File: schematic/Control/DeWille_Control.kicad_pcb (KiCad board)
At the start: 4 copper layers, 95 x 76.2 mm, 145 parts, among them J101 HN2x10, J102 HN2x10, J103 HN2x10, J201 SMA F ST PCB, J202 SMA F ST PCB, J501 Micro USB - KMMVX-SMT-BS-BTR, U201 KC2520K22.5792C1GE00, U202 KC2520K24.576C1GE00, U203 Si5344, U204 TPS79333-EP, U205 TPS73633DCQ, U206 TPS73618DCQ, U207 TPS79333-EP, U301 ESP32DevKit, U401 LFXP2-5E-5TN144, U402 IS61WV25616E, U403 TPS73633DCQ, U404 TPS79333-EP, U405 TLV74112PDBVR, U501 93C46C, U502 FT2232H, Y201 CX3225SB48, Y501 12MHz

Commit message: Interim commit
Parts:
- removed D501: Green, LED_SMD:LED_0805_2012Metric
- removed D502: Red, LED_SMD:LED_0805_2012Metric
- removed JP401: SolderJumper_2_Open, Jumper:SolderJumper-2_P1.3mm_Open_RoundedPad1.0x1.5mm
- removed R507, R510: 470, Resistor_SMD:R_0603_1608Metric
- removed REF** (x4): MountingHole_3.2mm_M3_DIN965_Pad, MountingHole:MountingHole_3.2mm_M3_DIN965_Pad
- removed RN401, RN501: RA1206 10k, Resistor_SMD:R_Array_Convex_4x0603
- added C439: 220uF/10V, Capacitor_SMD:C_Elec_8x6.2, F.Cu at (-6.35, 7.24)
- added C517: 100nF, Capacitor_SMD:C_0603_1608Metric, B.Cu at (-26.8, 15.5)
- added D101: Green, LED_SMD:LED_0805_2012Metric, F.Cu at (-44.5, 16.5)
- added D102: Red, LED_SMD:LED_0805_2012Metric, F.Cu at (-44.5, 19.1)
- added D103: Red, LED_SMD:LED_0805_2012Metric, F.Cu at (-44.5, 21.6)
- added D104: Red, LED_SMD:LED_0805_2012Metric, F.Cu at (-44.5, 24.1)
- added D105: Red, LED_SMD:LED_0805_2012Metric, F.Cu at (-44.5, 26.7)
- added H101: MountingHole, MountingHole:MountingHole_3.2mm_M3_Pad, F.Cu at (-43.5, -34.0)
- added H102: MountingHole, MountingHole:MountingHole_3.2mm_M3_Pad, F.Cu at (-43.5, 34.0)
- added H103: MountingHole, MountingHole:MountingHole_3.2mm_M3_Pad, F.Cu at (43.5, -34.0)
- added H104: MountingHole, MountingHole:MountingHole_3.2mm_M3_Pad, F.Cu at (43.5, 34.0)
- added R101: 470, Resistor_SMD:R_0603_1608Metric, F.Cu at (-40.6, 16.5)
- added R102: 470, Resistor_SMD:R_0603_1608Metric, F.Cu at (-40.6, 19.1)
- added R103: 470, Resistor_SMD:R_0603_1608Metric, F.Cu at (-40.6, 21.6)
- added R104: 470, Resistor_SMD:R_0603_1608Metric, F.Cu at (-40.6, 24.1)
- added R105: 470, Resistor_SMD:R_0603_1608Metric, F.Cu at (-40.6, 26.7)
- added R301: 10k, Resistor_SMD:R_0603_1608Metric, F.Cu at (-25.5, -17.9)
- added R302: 10k, Resistor_SMD:R_0603_1608Metric, F.Cu at (-25.5, -20.8)
- added R405: 10k, Resistor_SMD:R_0603_1608Metric, F.Cu at (4.83, 8.89)
- added R406: 10k, Resistor_SMD:R_0603_1608Metric, F.Cu at (-2.67, 49.4)
- added R407: 10k, Resistor_SMD:R_0603_1608Metric, F.Cu at (-2.67, 50.8)
- added R408: 10k, Resistor_SMD:R_0603_1608Metric, F.Cu at (-2.67, 52.2)
- added R409: 10k, Resistor_SMD:R_0603_1608Metric, F.Cu at (-2.67, 53.6)
- added SW301: SW_DIP_x02, Package_DIP:DIP-4_W7.62mm, F.Cu at (-36.4, -20.4)
- added TP401: TestPoint, TestPoint:TestPoint_Pad_D1.0mm, F.Cu at (10.3, 0.25)
- C506, C507, C509, C510, C511, C512, C513, C514, C515, C516: moved to B.Cu
- J501: footprint Zmei_Footprints:USB_MICRO_KMMVX-SMT-BS-BTR -> Zmei_Footprints:USB_MICRO_207A-BBA0-R
- U402: value IS61WV25616E -> IS61WV5128FBLL
- moved J501 62.2 mm to (-20.1, 33.3)
- moved C421 59.5 mm to (38.1, 26.2), turned to 270 degrees
- moved U502 57.5 mm to (-21.6, 17.8), turned to 90 degrees
- moved U405 53.9 mm to (22.7, 54.6)
- moved C505 53.6 mm to (-20.7, 27.7), turned to 270 degrees
- moved C410 49.6 mm to (25.4, 48.3)
- moved C510 47.8 mm to (-19.8, 23.0), turned to 90 degrees
- moved C414 47.7 mm to (36.2, 26.2), turned to 270 degrees
- moved C513 45.4 mm to (-16.4, 20.1), turned to 180 degrees
- moved L502 44.3 mm to (-24.9, 31.6), turned to 90 degrees
- moved C416 44.1 mm to (22.7, 52.2)
- moved L501 43.2 mm to (-18.8, 27.7), turned to 90 degrees
- moved R508 42.2 mm to (-28.4, 31.8)
- moved L401 42.0 mm to (21.0, 45.1)
- moved L402 42.0 mm to (25.4, 45.1)
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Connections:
- net /Control/RX renamed /RX
- net /Control/TX renamed /TX
- net /SignalProcessing/D2 renamed /SignalProcessing/IO0
- net /SignalProcessing/D3 renamed /SignalProcessing/IO1
- net /SignalProcessing/D4 renamed /SignalProcessing/IO2
- net /SignalProcessing/D5 renamed /SignalProcessing/IO3
- net /SignalProcessing/D6 renamed /SignalProcessing/~WE~
- net Net-(U301-Pad14) renamed /Control/~RST_FPGA~
- C417 pad 2: /SignalProcessing/+3V3_FPGA -> /SignalProcessing/+3V3_IO
- C502 pad 2: Net-(C502-Pad2) -> /SignalProcessing/+3V3_IO
- C505 pad 1: /Usb/+1V8_USBCORE -> Net-(C505-Pad1)
- C505 pad 2: GNDA -> GND
- C507 pad 1: /Usb/+1V8_USBCORE -> Net-(C505-Pad1)
- C507 pad 2: GNDA -> GND
- C508 pad 2: GNDA -> GND
- C509 pad 2: GNDA -> GND
- C510 pad 2: GNDA -> GND
- C511 pad 2: GNDA -> GND
- C512 pad 2: GNDA -> GND
- C513 pad 2: GNDA -> GND
- C514 pad 2: GNDA -> GND
- C515 pad 2: GNDA -> GND
- C516 pad 2: GNDA -> GND
- J101 pad 1: GND -> /Clock/+5V
- J101 pad 10: /SignalProcessing/I2S2_DATA_IN -> /SignalProcessing/I2S2_SCK_IN
- J101 pad 14: /SignalProcessing/I2S_LRCK_IN -> /SignalProcessing/I2S2_LRCK_IN
- J101 pad 16: /SignalProcessing/SPDIF2_IN -> /SignalProcessing/I2S2_DATA_IN
- J101 pad 18: /SignalProcessing/SPDIF1_IN -> /SignalProcessing/SPDIF2_IN
- J101 pad 19: GND -> /Clock/+5V
- J101 pad 2: /Clock/+5V -> /SignalProcessing/I2S1_SCK_IN
- J101 pad 20: /Clock/+5V -> /SignalProcessing/SPDIF1_IN
- J101 pad 4: /SignalProcessing/I2S1_DATA_IN -> /SignalProcessing/I2S1_BCK_IN
- J101 pad 6: /SignalProcessing/I2S1_BCK_IN -> /SignalProcessing/I2S1_LRCK_IN
- J101 pad 8: /SignalProcessing/I2S1_LRCK_IN -> /SignalProcessing/I2S1_DATA_IN
- L501 pad 2: /Usb/+1V8_USBCORE -> Net-(C505-Pad1)
- R403 pad 1: /SignalProcessing/+3V3_FPGA -> /SignalProcessing/+3V3_IO
- R404 pad 1: /SignalProcessing/+3V3_FPGA -> /SignalProcessing/+3V3_IO
- R501 pad 1: Net-(C502-Pad2) -> /SignalProcessing/+3V3_IO
- R502 pad 1: Net-(C502-Pad2) -> /SignalProcessing/+3V3_IO
- R504 pad 1: Net-(C502-Pad2) -> /SignalProcessing/+3V3_IO
- U301 pad 15: Net-(U301-Pad15) -> /~DACL_RST~
- U301 pad 16: Net-(U301-Pad16) -> /~DACR_RST~
- U301 pad 24: /~DACR_RST~ -> Net-(U301-Pad24)
- U301 pad 25: /~DACL_RST~ -> /~CLK_RST_
- U301 pad 5: Net-(U301-Pad5) -> /Control/LED1
- U301 pad 6: Net-(U301-Pad6) -> /Control/LED2
- U401 pad 10: /SignalProcessing/A16 -> Net-(U401-Pad10)
- U401 pad 116: Net-(U401-Pad116) -> /FPGA_SCK
- U401 pad 120: /FPGA_SCK -> /SignalProcessing/I2S1_SCK_IN
- U401 pad 122: Net-(U401-Pad122) -> /SignalProcessing/I2S1_BCK_IN
- U401 pad 123: Net-(U401-Pad123) -> /SignalProcessing/I2S1_LRCK_IN
- U401 pad 125: Net-(U401-Pad125) -> /SignalProcessing/I2S1_DATA_IN
- U401 pad 129: Net-(U401-Pad129) -> /SignalProcessing/I2S2_SCK_IN
- U401 pad 131: Net-(U401-Pad131) -> /SignalProcessing/I2S2_BCK_IN
- U401 pad 132: Net-(U401-Pad132) -> /SignalProcessing/I2S2_LRCK_IN
- U401 pad 134: Net-(U401-Pad134) -> /SignalProcessing/I2S2_DATA_IN
- U401 pad 15: /SignalProcessing/A15 -> Net-(U401-Pad15)
- U401 pad 17: /SignalProcessing/~RAM_OE~ -> /SignalProcessing/~RST~
- U401 pad 21: /SignalProcessing/~RAM_UB~ -> /SignalProcessing/FPGA_LED
- U401 pad 22: /SignalProcessing/~RAM_LB~ -> Net-(U401-Pad22)
- U401 pad 27: /SignalProcessing/D15 -> /SignalProcessing/A20
- U401 pad 28: /SignalProcessing/D14 -> /SignalProcessing/A18
- U401 pad 29: /SignalProcessing/D13 -> /SignalProcessing/A17
- U401 pad 30: /SignalProcessing/D12 -> /SignalProcessing/A16
- U401 pad 31: /SignalProcessing/D11 -> /SignalProcessing/A15
- U401 pad 32: /SignalProcessing/D10 -> /SignalProcessing/~OE~
- U401 pad 35: /SignalProcessing/D9 -> /SignalProcessing/IO7
- U401 pad 36: /SignalProcessing/D8 -> /SignalProcessing/IO6
- U401 pad 37: /SignalProcessing/A18 -> /SignalProcessing/IO5
- U401 pad 38: /SignalProcessing/A14 -> /SignalProcessing/IO4
- U401 pad 39: /SignalProcessing/A13 -> /SignalProcessing/A14
- U401 pad 40: /SignalProcessing/A12 -> /SignalProcessing/A13
- U401 pad 43: /SignalProcessing/A11 -> /SignalProcessing/A12
- U401 pad 44: /SignalProcessing/A10 -> /SignalProcessing/A11
- U401 pad 45: /SignalProcessing/A0 -> /SignalProcessing/A19
- U401 pad 46: /SignalProcessing/A1 -> /SignalProcessing/A10
- U401 pad 47: /SignalProcessing/A2 -> /SignalProcessing/A0
- U401 pad 48: /SignalProcessing/A3 -> /SignalProcessing/A1
- U401 pad 50: /SignalProcessing/A4 -> /SignalProcessing/A2
- U401 pad 52: /SignalProcessing/~RAM_CS~ -> /SignalProcessing/A3
- U401 pad 53: /SignalProcessing/D0 -> /SignalProcessing/A4
- U401 pad 54: /SignalProcessing/D1 -> /~FPGA_CS~
- U401 pad 6: /SignalProcessing/A17 -> Net-(U401-Pad6)
- U401 pad 62: /SignalProcessing/D7 -> /SignalProcessing/A5
- U401 pad 65: /SignalProcessing/~RAM_WE~ -> /SignalProcessing/A6
- U401 pad 66: /SignalProcessing/A5 -> /SignalProcessing/A7
- U401 pad 69: /SignalProcessing/A6 -> /SignalProcessing/A8
- U401 pad 70: /SignalProcessing/A7 -> /SignalProcessing/A9
- U401 pad 71: /SignalProcessing/A8 -> Net-(U401-Pad71)
- U401 pad 72: /SignalProcessing/A9 -> Net-(U401-Pad72)
- U401 pad 83: /SignalProcessing/+3V3_FPGA -> /SignalProcessing/+3V3_IO
- U402 pad 1: /SignalProcessing/A0 -> Net-(U402-Pad1)
- U402 pad 16: /SignalProcessing/D7 -> /SignalProcessing/A5
- U402 pad 17: /SignalProcessing/~RAM_WE~ -> /SignalProcessing/A6
- U402 pad 18: /SignalProcessing/A5 -> /SignalProcessing/A7
- U402 pad 19: /SignalProcessing/A6 -> /SignalProcessing/A8
- U402 pad 2: /SignalProcessing/A1 -> Net-(U402-Pad2)
- U402 pad 20: /SignalProcessing/A7 -> /SignalProcessing/A9
- U402 pad 21: /SignalProcessing/A8 -> Net-(U402-Pad21)
- U402 pad 22: /SignalProcessing/A9 -> Net-(U402-Pad22)
- U402 pad 23: /SignalProcessing/A10 -> Net-(U402-Pad23)
- U402 pad 24: /SignalProcessing/A11 -> Net-(U402-Pad24)
- U402 pad 25: /SignalProcessing/A12 -> /SignalProcessing/A19
- U402 pad 26: /SignalProcessing/A13 -> /SignalProcessing/A10
- U402 pad 27: /SignalProcessing/A14 -> /SignalProcessing/A11
- U402 pad 28: /SignalProcessing/A18 -> /SignalProcessing/A12
- U402 pad 29: /SignalProcessing/D8 -> /SignalProcessing/A13
- U402 pad 3: /SignalProcessing/A2 -> /SignalProcessing/A0
- U402 pad 30: /SignalProcessing/D9 -> /SignalProcessing/A14
- U402 pad 31: /SignalProcessing/D10 -> /SignalProcessing/IO4
- U402 pad 32: /SignalProcessing/D11 -> /SignalProcessing/IO5
- U402 pad 35: /SignalProcessing/D12 -> /SignalProcessing/IO6
- U402 pad 36: /SignalProcessing/D13 -> /SignalProcessing/IO7
- U402 pad 37: /SignalProcessing/D14 -> /SignalProcessing/~OE~
- U402 pad 38: /SignalProcessing/D15 -> /SignalProcessing/A15
- U402 pad 39: /SignalProcessing/~RAM_LB~ -> /SignalProcessing/A16
- U402 pad 4: /SignalProcessing/A3 -> /SignalProcessing/A1
- U402 pad 40: /SignalProcessing/~RAM_UB~ -> /SignalProcessing/A17
- U402 pad 41: /SignalProcessing/~RAM_OE~ -> /SignalProcessing/A18
- U402 pad 42: /SignalProcessing/A15 -> /SignalProcessing/A20
- U402 pad 43: /SignalProcessing/A16 -> Net-(U402-Pad43)
- U402 pad 44: /SignalProcessing/A17 -> Net-(U402-Pad44)
- U402 pad 5: /SignalProcessing/A4 -> /SignalProcessing/A2
- U402 pad 6: /SignalProcessing/~RAM_CS~ -> /SignalProcessing/A3
- U402 pad 7: /SignalProcessing/D0 -> /SignalProcessing/A4
- U402 pad 8: /SignalProcessing/D1 -> /~FPGA_CS~
- U501 pad 6: Net-(C502-Pad2) -> /SignalProcessing/+3V3_IO
- U501 pad 8: Net-(C502-Pad2) -> /SignalProcessing/+3V3_IO
- U502 pad 54: Net-(D501-Pad1) -> /Usb/RXLED
- U502 pad 55: Net-(D502-Pad1) -> /Usb/TXLED
- U502 pad 9: /Usb/+1V8_USBCORE -> Net-(C505-Pad1)
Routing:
- net GND: track 15.1 -> 207.7 mm, vias 50 -> 155
- net /SignalProcessing/+3V3_IO: track 16.9 -> 106.5 mm, vias 12 -> 20
- net /SignalProcessing/I2S1_BCK_IN: track 0.00 -> 82.2 mm, vias 0 -> 1
- net /Clock/+5V: track 0.00 -> 79.7 mm
- net /MISO: track 0.00 -> 76.2 mm
- net /SCLK: track 0.00 -> 75.7 mm
- net /SignalProcessing/I2S1_LRCK_IN: track 0.00 -> 74.8 mm, vias 0 -> 1
- net /SignalProcessing/I2S1_SCK_IN: track 0.00 -> 72.9 mm, vias 0 -> 1
- net /SignalProcessing/I2S1_DATA_IN: track 0.00 -> 70.2 mm, vias 0 -> 1
- net /SignalProcessing/I2S2_SCK_IN: track 0.00 -> 66.1 mm, vias 0 -> 1
- net /MOSI: track 0.00 -> 65.4 mm
- net /SignalProcessing/I2S2_BCK_IN: track 0.00 -> 65.1 mm, vias 0 -> 1
- net /SignalProcessing/I2S2_LRCK_IN: track 0.00 -> 64.2 mm, vias 0 -> 1
- net /SignalProcessing/I2S2_DATA_IN: track 0.00 -> 63.2 mm, vias 0 -> 1
- net /SignalProcessing/FPGA_LED: track 0.00 -> 43.2 mm
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- added copper zone on B.Cu, net /SignalProcessing/+3V3_IO
- added copper zone on In1.Cu, net GND

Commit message: Routing complete
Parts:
- removed C415, C422: 10uF, Capacitor_SMD:C_0603_1608Metric
- removed C419: 10nF, Capacitor_SMD:C_0603_1608Metric
- removed JP105: , Connector_PinHeader_2.54mm:PinHeader_1x02_P2.54mm_Vertical
- removed U404: TPS79333-EP, Package_TO_SOT_SMD:SOT-23-5
- added C440: 100uF/10V, Capacitor_SMD:C_Elec_6.3x5.4, F.Cu at (36.1, 6.99)
- added D106: SM6T6V8CA, Diode_SMD:D_SMB, F.Cu at (-34.7, -16.3)
- added F101: PFMF.050.2, Fuse:Fuse_1812_4532Metric, F.Cu at (-42.3, -16.3)
- added J401: JTAG, Connector_PinHeader_2.54mm:PinHeader_1x06_P2.54mm_Vertical, F.Cu at (23.5, 35.6)
- C413: value 10nF -> 47uF/6.3V; footprint Capacitor_SMD:C_0603_1608Metric -> Capacitor_Tantalum_SMD:CP_EIA-3528-12_Kemet-T
- C424, C439: value 220uF/10V -> 100uF/10V; footprint Capacitor_SMD:C_Elec_8x6.2 -> Capacitor_SMD:C_Elec_6.3x5.4
- JP101, JP102, JP103, JP104: footprint Connector_PinHeader_2.54mm:PinHeader_1x02_P2.54mm_Vertical -> Jumper:SolderJumper-2_P1.3mm_Bridged_RoundedPad1.0x1.5mm
- moved C416 49.9 mm to (-6.22, 11.6)
- moved C420 49.9 mm to (-6.22, 16.4)
- moved C423 49.9 mm to (-8.89, 13.7)
- moved U405 49.9 mm to (-6.22, 14.0)
- moved L402 43.9 mm to (-2.41, 11.2), turned to 180 degrees
- moved C439 41.0 mm to (27.8, 29.8), turned to 225 degrees
- moved C410 39.9 mm to (1.24, 16.5), turned to 0 degrees
- moved R301 36.0 mm to (6.35, -34.7), turned to 90 degrees
- moved R302 32.4 mm to (3.81, -34.7), turned to 90 degrees
- moved C413 31.9 mm to (-2.41, 14.7), turned to 270 degrees
- moved R406 31.9 mm to (26.0, 35.6), turned to 270 degrees
- moved C412 27.5 mm to (1.24, 15.1)
- moved JP101 25.8 mm to (-14.1, 25.9)
- moved L401 22.3 mm to (32.0, 25.7), turned to 225 degrees
- moved R409 21.1 mm to (8.26, 35.6), turned to 270 degrees
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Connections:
- C413 pad 1: GND -> /SignalProcessing/+1V2_FPGA
- C413 pad 2: /SignalProcessing/+3V3_FPGA -> GND
- C423 pad 2: /Clock/+5V -> /SignalProcessing/+3V3_IO
- J101 pad 1: /Clock/+5V -> Net-(F101-Pad2)
- J101 pad 18: /SignalProcessing/SPDIF2_IN -> /SignalProcessing/SPDIF1_IN
- J101 pad 19: /Clock/+5V -> Net-(F101-Pad2)
- J101 pad 20: /SignalProcessing/SPDIF1_IN -> /SignalProcessing/SPDIF2_IN
- L401 pad 2: Net-(C415-Pad2) -> /SignalProcessing/+3V3_IO
- U301 pad 10: Net-(U301-Pad10) -> /Control/~FPGA_INIT~
- U301 pad 15: /~DACL_RST~ -> /~FPGA_CS~
- U301 pad 16: /~DACR_RST~ -> /SignalProcessing/DONE
- U301 pad 17: Net-(U301-Pad17) -> /Control/~FPGA_PROGRAM~
- U301 pad 25: /~CLK_RST_ -> /~DACL_CS~
- U301 pad 26: /Control/~FPGA_INIT~ -> /~DACL_RST~
- U301 pad 27: /Control/~FPGA_PROGRAM~ -> /~DACR_CS~
- U301 pad 28: /~CLK_CS~ -> /~DACR_RST~
- U301 pad 29: /~FPGA_CS~ -> /~CLK_CS~
- U301 pad 30: /~DACR_CS~ -> /~CLK_RST_
- U301 pad 31: /~DACL_CS~ -> Net-(U301-Pad31)
- U301 pad 33: /SignalProcessing/DONE -> Net-(U301-Pad33)
- U401 pad 1: Net-(U401-Pad1) -> /SignalProcessing/FPGA_LED
- U401 pad 138: Net-(U401-Pad138) -> /SignalProcessing/SPDIF1_IN
- U401 pad 142: Net-(U401-Pad142) -> /SignalProcessing/SPDIF2_IN
- U401 pad 17: /SignalProcessing/~RST~ -> /Control/~RST_FPGA~
- U401 pad 21: /SignalProcessing/FPGA_LED -> Net-(U401-Pad21)
- U401 pad 54: /~FPGA_CS~ -> /SignalProcessing/~CS~
- U402 pad 8: /~FPGA_CS~ -> /SignalProcessing/~CS~
- U405 pad 1: /Clock/+5V -> /SignalProcessing/+3V3_IO
- U405 pad 3: /Clock/+5V -> /SignalProcessing/+3V3_IO
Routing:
- net /MOSI: track 65.4 -> 190.5 mm, vias 0 -> 6
- net /~DACR_RST~: track 0.00 -> 111.1 mm, vias 0 -> 1
- net /SignalProcessing/+3V3_FPGA: track 25.4 -> 134.8 mm, vias 6 -> 11
- net /SCLK: track 75.7 -> 182.7 mm, vias 0 -> 4
- net GND: track 207.7 -> 314.5 mm, vias 155 -> 169
- net /MISO: track 76.2 -> 179.3 mm, vias 0 -> 4
- net /SignalProcessing/+1V2_FPGA: track 10.9 -> 113.4 mm, vias 4 -> 7
- net /~DACR_CS~: track 24.4 -> 106.9 mm, vias 0 -> 1
- net /~DACL_RST~: track 0.00 -> 73.3 mm, vias 0 -> 1
- net /~DACL_CS~: track 0.00 -> 69.0 mm, vias 0 -> 1
- net /SignalProcessing/TDO: track 10.1 -> 76.1 mm, vias 0 -> 1
- net /SignalProcessing/TDI: track 8.54 -> 72.6 mm, vias 0 -> 1
- net /SignalProcessing/TMS: track 11.3 -> 72.6 mm, vias 0 -> 1
- net /SignalProcessing/SPDIF1_IN: track 1.20 -> 60.9 mm, vias 0 -> 1
- net /SignalProcessing/SPDIF2_IN: track 0.00 -> 58.7 mm, vias 0 -> 1
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- added copper zone on B.Cu, net /Clock/+5V
- added copper zone on B.Cu, net /Usb/+1V8_USBCORE
- added copper zone on B.Cu, net GND
- added copper zone on B.Cu, net Net-(F101-Pad2)

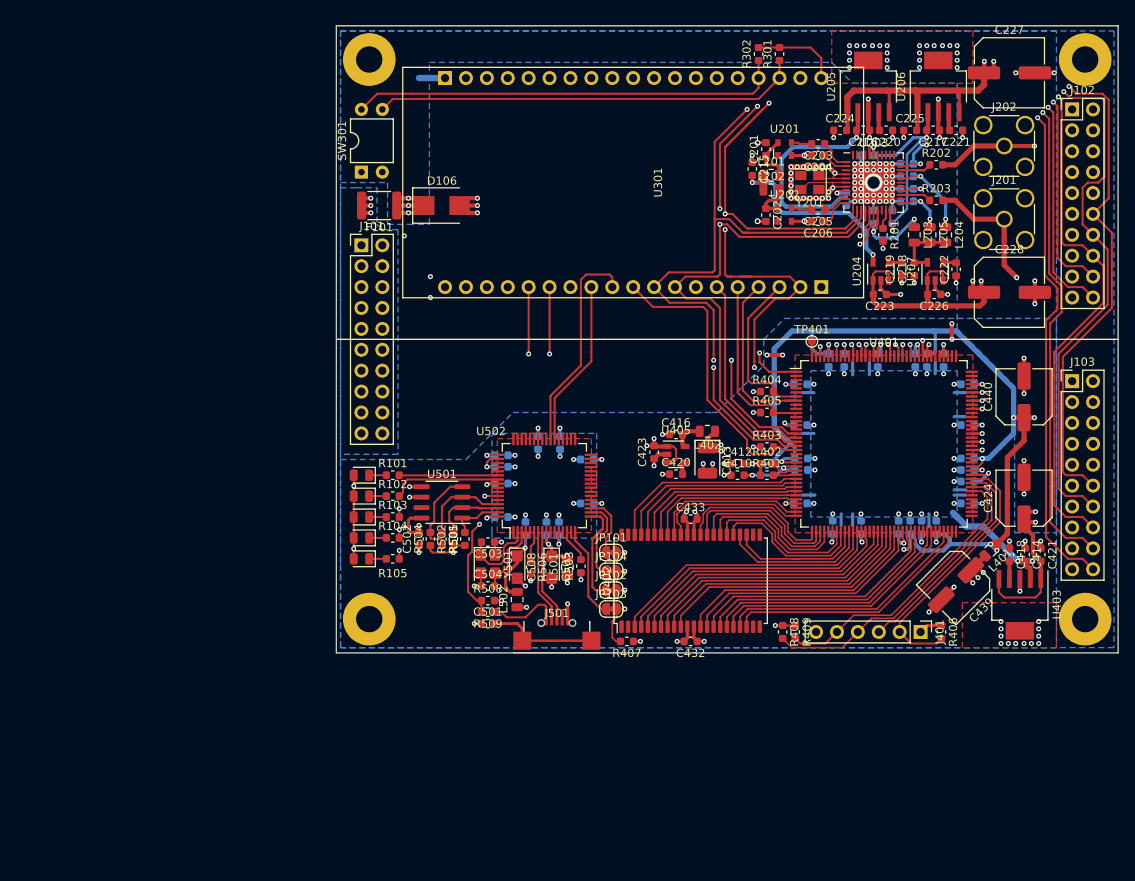
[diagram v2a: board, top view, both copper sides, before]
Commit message: Add source termination resistors to I2S output lines. Arrange top silk information.
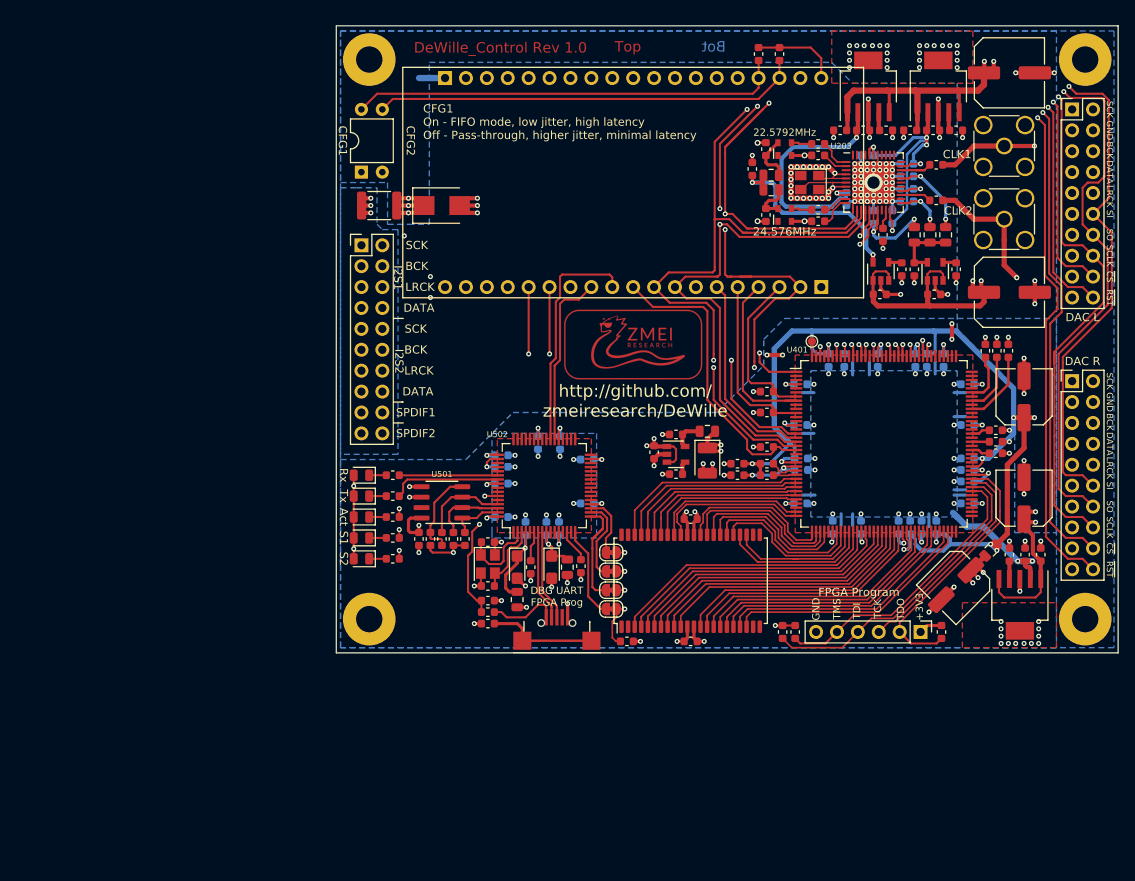
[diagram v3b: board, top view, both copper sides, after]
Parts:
- added R410: 39, Resistor_SMD:R_0603_1608Metric, F.Cu at (31.4, 1.40)
- added R411: 39, Resistor_SMD:R_0603_1608Metric, F.Cu at (32.8, 1.40)
- added R412: 39, Resistor_SMD:R_0603_1608Metric, F.Cu at (34.2, 1.40)
- added R413: 39, Resistor_SMD:R_0603_1608Metric, F.Cu at (32.6, 11.0)
- added R414: 39, Resistor_SMD:R_0603_1608Metric, F.Cu at (32.6, 12.4)
- added R415: 39, Resistor_SMD:R_0603_1608Metric, F.Cu at (32.6, 13.8)
- added U101: Logo, Zmei_Footprints:Zmei-logo-small-inverted_nosilk, F.Cu at (-11.4, 0.64)
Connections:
- U401 pad 101: /DACL_DATA -> Net-(R411-Pad1)
- U401 pad 103: /DACL_BCK -> Net-(R410-Pad1)
- U401 pad 89: /DACR_LRCK -> Net-(R415-Pad1)
- U401 pad 91: /DACR_DATA -> Net-(R414-Pad1)
- U401 pad 93: /DACR_BCK -> Net-(R413-Pad1)
- U401 pad 99: /DACL_LRCK -> Net-(R412-Pad1)
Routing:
- net /DACL_LRCK: track 36.7 -> 26.2 mm
- net /DACL_DATA: track 38.0 -> 28.7 mm
- net Net-(R412-Pad1): track 0.00 -> 8.97 mm
- net /DACL_BCK: track 39.4 -> 31.9 mm
- net Net-(R411-Pad1): track 0.00 -> 7.38 mm
- net Net-(R410-Pad1): track 0.00 -> 6.10 mm
- net /DACR_LRCK: track 16.5 -> 12.7 mm
- net /DACR_BCK: track 15.3 -> 11.7 mm
- net Net-(R413-Pad1): track 0.00 -> 2.31 mm
- net Net-(R415-Pad1): track 0.00 -> 2.30 mm
- net Net-(R414-Pad1): track 0.00 -> 1.78 mm
- net /TX: track 26.3 -> 28.0 mm
- net /DACR_DATA: track 15.9 -> 14.3 mm
- net /RX: track 20.3 -> 21.3 mm
- net /SignalProcessing/+3V3_FPGA: track 134.8 -> 135.4 mm
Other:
- board text added: "+3V3"
- board text added: "22.5792MHz"
- board text added: "24.576MHz"
- board text added: "Act"
- board text added: "BCK"
- board text added: "Bot"
- board text added: "Bot Mask"
- board text added: "CFG1"
- board text added: "CFG1 On - FIFO mode, low jitter, high latency Off - Pass-through, higher jitter, minimal latency"
- board text added: "CFG2"
- board text added: "CLK1"
- board text added: "CLK2"
- board text added: "DAC L"
- board text added: "DAC R"
- board text added: "DATA"
- board text added: "DBG UART FPGA Prog"
- board text added: "DeWille_Control Rev 1.0"
- board text added: "FPGA Program"
- board text added: "GND"
- board text added: "I2S1"
- board text added: "I2S2"
- board text added: "LRCK"
- board text added: "Mid 1"
- board text added: "Mid 2"
- board text added: "Rx"
- board text added: "S1"
- board text added: "S2"
- board text added: "SCK"
- board text added: "SCLK"
- board text added: "SI"
- board text added: "SO"
- board text added: "SPDIF1"
- board text added: "SPDIF2"
- board text added: "TCK"
- board text added: "TDI"
- board text added: "TDO"
- board text added: "TMS"
- board text added: "Top"
- board text added: "Top Mask"
- board text added: "Tx"
- board text added: "http://github.com/ zmeiresearch/DeWille"
- board text added: "~CS~"
- board text added: "~RST~"
- board text removed: "Layer 1 - Signal Layer 2 - GND Layer 3 - Imp. Controlled signals Layer 4 - Power Back side - Filter capacitors ONLY!"

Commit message: Arrange bottom silk screen. Remove obsolete files.
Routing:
- net /SignalProcessing/+3V3_IO: track 139.5 -> 138.1 mm
- net GND: vias 169 -> 194

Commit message: Add some testpads. Fix +3V3_FPGA track mix-up after termination addition.
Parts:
- added TP101: TestPoint_+3V3, TestPoint:TestPoint_THTPad_D2.0mm_Drill1.0mm, F.Cu at (-36.2, 27.9)
- added TP102: TestPoint_GND, TestPoint:TestPoint_THTPad_D2.0mm_Drill1.0mm, F.Cu at (-36.2, 34.3)
- added TP103: TestPoint_GND, TestPoint:TestPoint_THTPad_D2.0mm_Drill1.0mm, F.Cu at (45.7, 0.00)
- added TP402: TestPoint_free2, TestPoint:TestPoint_Pad_D1.0mm, F.Cu at (31.8, 9.40)
- added TP403: TP_free1, TestPoint:TestPoint_Pad_D1.0mm, F.Cu at (6.48, 3.30)
- TP401: value TestPoint -> TestPoint_UPLLTL
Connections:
- U401 pad 1: /SignalProcessing/FPGA_LED -> Net-(TP403-Pad1)
- U401 pad 2: Net-(U401-Pad2) -> /SignalProcessing/FPGA_LED
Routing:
- net Net-(TP402-Pad1): track 0.00 -> 2.22 mm
- net Net-(TP403-Pad1): track 0.00 -> 2.18 mm
- net /SignalProcessing/+3V3_FPGA: track 135.4 -> 136.1 mm

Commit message: Add decoupling cap between +5V and GND
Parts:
- added C101: 1nF, Capacitor_SMD:C_0603_1608Metric, B.Cu at (40.1, 0.00)
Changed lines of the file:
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@@
     (tracks 1969)
     (zones 0)
-    (modules 170)
+    (modules 171)
     (nets 254)
   )
@@
   (layers
     (0 F.Cu signal)
-    (1 In1.Cu signal hide)
+    (1 In1.Cu signal)
     (2 In2.Cu signal)
     (31 B.Cu signal)
@@
     (add_net "Net-(U502-Pad60)")
   )
+  (module Capacitor_SMD:C_0603_1608Metric (layer B.Cu)
+    (at 40.132 0 180)
+    (descr "Capacitor SMD 0603 (1608 Metric), square (rectangular) end terminal, IPC_7351 nominal, (Body size source: http://www.tortai-tech.com/upload/download/2011102023233369053.pdf), generated with kicad-footprint-generator")
+    (tags capacitor)
+    (attr smd)
+    (fp_text reference C101 (at 0 1.43) (layer B.SilkS) hide
+      (effects (font (size 1 1) (thickness 0.15)) (justify mirror))
+    )
+    (fp_text value 1nF (at 0 -1.43) (layer B.Fab)
+      (effects (font (size 1 1) (thickness 0.15)) (justify mirror))
+    )
+    (fp_text user %R (at 0 0) (layer B.Fab)
+      (effects (font (size 0.4 0.4) (thickness 0.06)) (justify mirror))
+    )
+    (fp_line (start 1.48 -0.73) (end -1.48 -0.73) (layer B.CrtYd) (width 0.05))
+    (fp_line (start 1.48 0.73) (end 1.48 -0.73) (layer B.CrtYd) (width 0.05))
+    (fp_line (start -1.48 0.73) (end 1.48 0.73) (layer B.CrtYd) (width 0.05))
+    (fp_line (start -1.48 -0.73) (end -1.48 0.73) (layer B.CrtYd) (width 0.05))
+    (fp_line (start -0.162779 -0.51) (end 0.162779 -0.51) (layer B.SilkS) (width 0.12))
+    (fp_line (start -0.162779 0.51) (end 0.162779 0.51) (layer B.SilkS) (width 0.12))
+    (fp_line (start 0.8 -0.4) (end -0.8 -0.4) (layer B.Fab) (width 0.1))
+    (fp_line (start 0.8 0.4) (end 0.8 -0.4) (layer B.Fab) (width 0.1))
+    (fp_line (start -0.8 0.4) (end 0.8 0.4) (layer B.Fab) (width 0.1))
+    (fp_line (start -0.8 -0.4) (end -0.8 0.4) (layer B.Fab) (width 0.1))
+    (pad 2 smd roundrect (at 0.7875 0 180) (size 0.875 0.95) (layers B.Cu B.Paste B.Mask) (roundrect_rratio 0.25)
+      (net 21 /Clock/+5V))
+    (pad 1 smd roundrect (at -0.7875 0 180) (size 0.875 0.95) (layers B.Cu B.Paste B.Mask) (roundrect_rratio 0.25)
+      (net 1 GND))
+    (model ${KISYS3DMOD}/Capacitor_SMD.3dshapes/C_0603_1608Metric.wrl
+      (at (xyz 0 0 0))
+      (scale (xyz 1 1 1))
+      (rotate (xyz 0 0 0))
+    )
+  )
   (module TestPoint:TestPoint_THTPad_D2.0mm_Drill1.0mm (layer F.Cu)

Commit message: Swap BCK and LRCK outputs. Misc small touch-ups on the board
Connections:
- J102 pad 10: /DACL_LRCK -> /DACL_BCK
- J102 pad 6: /DACL_BCK -> /DACL_LRCK
- J103 pad 10: /DACR_LRCK -> /DACR_BCK
- J103 pad 6: /DACR_BCK -> /DACR_LRCK
- R410 pad 2: /DACL_BCK -> /DACL_LRCK
- R412 pad 2: /DACL_LRCK -> /DACL_BCK
- R413 pad 2: /DACR_BCK -> /DACR_LRCK
- R415 pad 2: /DACR_LRCK -> /DACR_BCK
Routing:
- net /DACL_LRCK: track 26.2 -> 31.9 mm
- net /DACL_BCK: track 31.9 -> 26.2 mm
- net /DACR_LRCK: track 12.7 -> 11.7 mm
- net /DACR_BCK: track 11.7 -> 12.7 mm
